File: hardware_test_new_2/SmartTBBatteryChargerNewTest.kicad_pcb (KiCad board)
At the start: 4 copper layers, 100 x 100 mm, 260 parts, among them J10 XT60_MALE, J3 XT60_MALE, J4 XT60_MALE, J5 XT60_MALE, J6 XT60_MALE, J7 Conn_SWD, J8 Conn_01x02, J9 XT60_MALE, Q3 AO3400A, Q4 BSC070N10NS5, Q5 BSC070N10NS5, Q6 BSC070N10NS5, Q7 BSC070N10NS5, Q8 BSC070N10NS5, Q9 BSC070N10NS5, SW1 SW_Push, SW2 SW_Push, SW3 SW_Push, SW4 SW_Push, SW5 SW_Push, SW6 SW_Push, U1 RY8411, U10 INA180A1, U11 INA180A1, U12 FD6288Q, U2 RS3236, U3 RY8411, U4 STM32G474RBTx, U5 INA180A1, U6 FD6288Q, U7 INA180A1, U8 INA180A1, U9 INA180A1

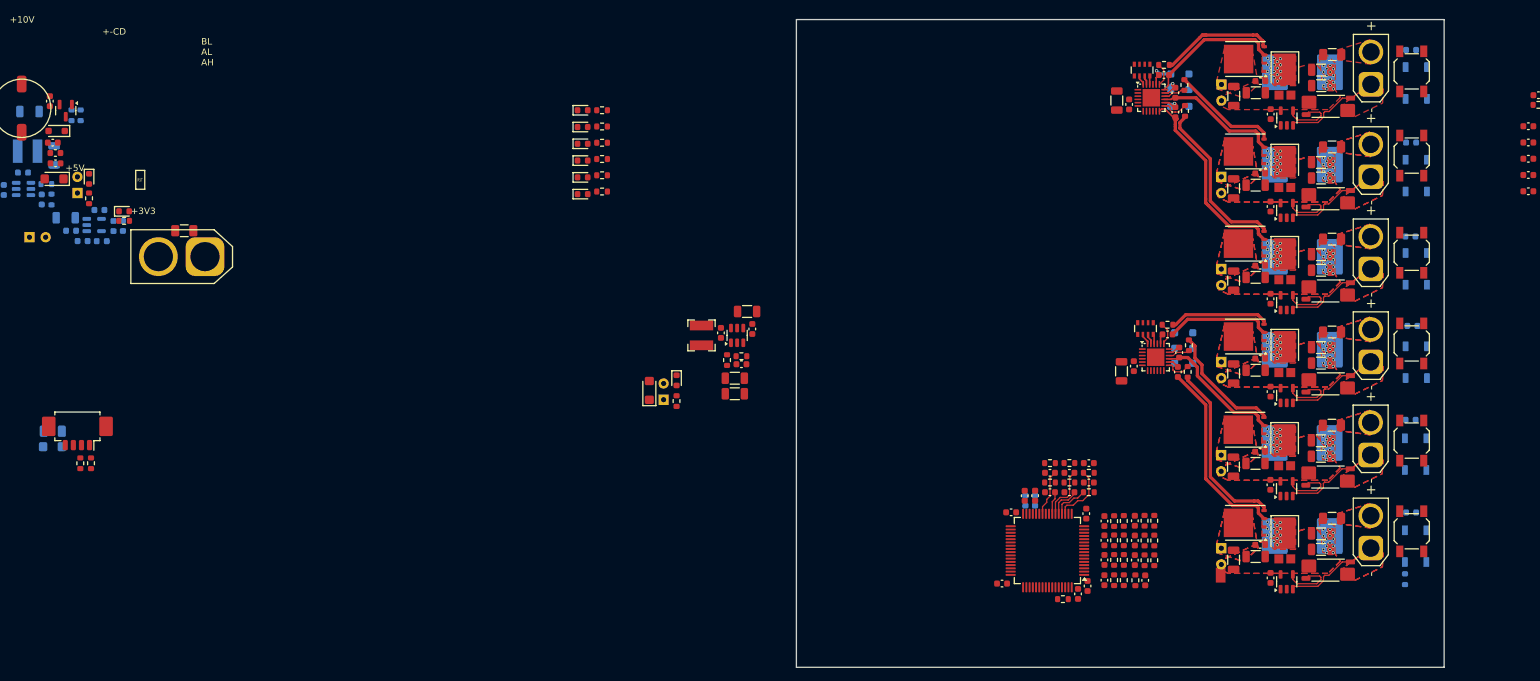
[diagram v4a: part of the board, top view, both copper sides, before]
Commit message: rearrange layout
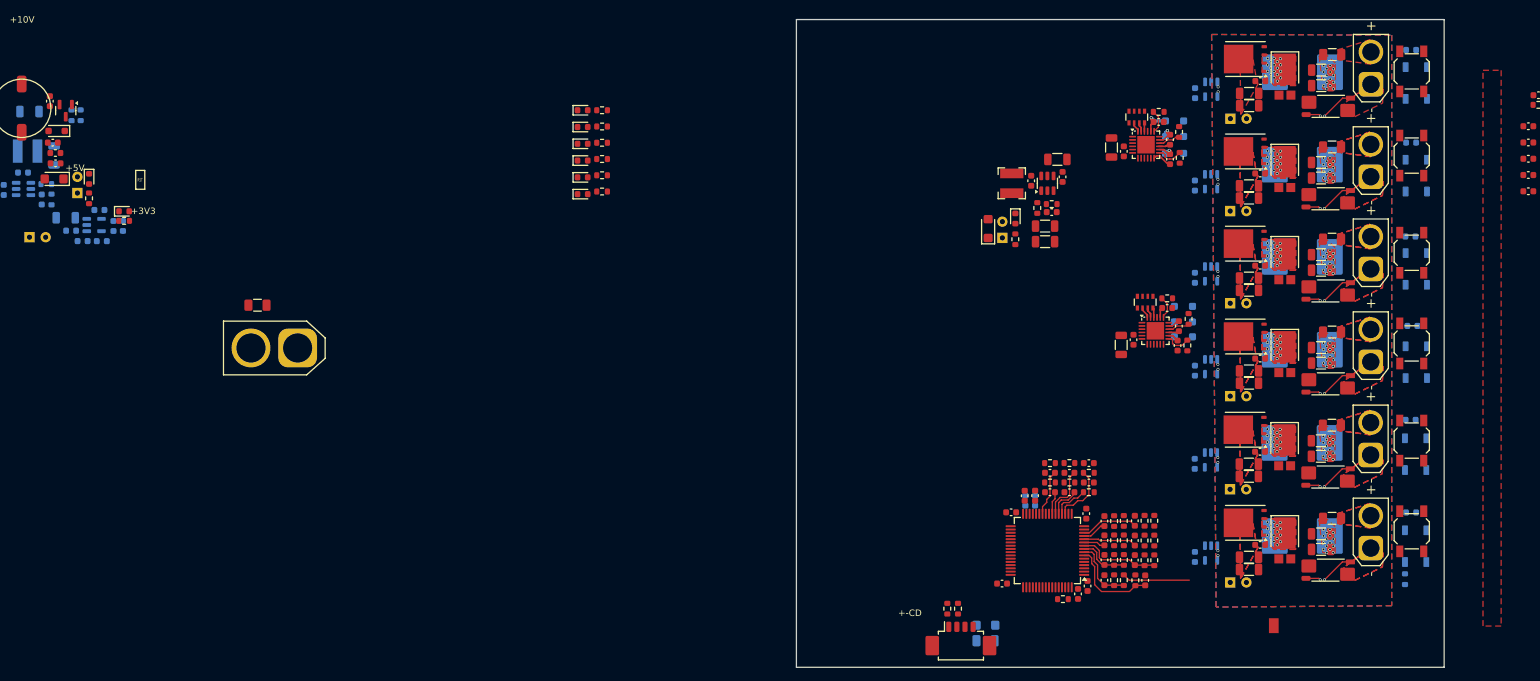
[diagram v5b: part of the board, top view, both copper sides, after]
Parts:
- C44, C51, C67, C84, C85, C86, U10, U11, U5, U7, U8, U9: moved to B.Cu
- moved F7 147.6 mm to (186.2, 147.9), turned to 180 degrees
- moved D15 146.7 mm to (186.2, 145.5), turned to 180 degrees
- moved J7 140.3 mm to (182.4, 148.2), turned to 0 degrees
- moved R36 137.3 mm to (181.9, 142.9), turned to -90 degrees
- moved R37 134.1 mm to (180.3, 142.9), turned to -90 degrees
- moved D17 58.0 mm to (190.8, 82.7)
- moved R19 58.0 mm to (190.8, 85.9)
- moved C20 58.0 mm to (188.8, 85.7)
- moved D1 58.0 mm to (186.6, 84.3)
- moved C1 53.3 mm to (197.3, 73.6)
- moved C14 53.3 mm to (196.4, 81.7)
- moved C16 53.3 mm to (195.4, 86.3)
- moved C6 53.3 mm to (198.1, 76.3)
- moved L1 53.3 mm to (190.2, 77.3)
- moved R1 53.3 mm to (196.4, 80.5)
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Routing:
- net CHC2_SW: track 29.5 -> 0.00 mm
- net Net-(Q9-G): track 27.6 -> 0.00 mm
- net CHB1_SW: track 30.3 -> 3.13 mm
- net Net-(Q6-G): track 25.8 -> 0.00 mm
- net CHA1_SW: track 21.1 -> 0.00 mm
- net Net-(Q8-G): track 18.6 -> 0.00 mm
- net CHC1_SW: track 20.0 -> 1.43 mm
- net Net-(Q4-G): track 17.7 -> 0.00 mm
- net CHA2_SW: track 19.2 -> 1.65 mm
- net Net-(Q5-G): track 16.7 -> 0.00 mm
- net CHB2_SW: track 16.4 -> 0.00 mm
- net Net-(Q7-G): track 15.6 -> 0.00 mm
- net Net-(U4-PG10): track 0.00 -> 14.3 mm
- net CHC1_VS: track 0.00 -> 12.8 mm
- net /ChannelC2/CH_SHUNT+: track 11.2 -> 23.6 mm, vias 0 -> 2
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- added copper zone on B.Cu, net GNDPWR
- added copper zone on In1.Cu, net GNDPWR
- added copper zone on In2.Cu, net GNDPWR
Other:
- board text removed: "BL AL AH"
- board text removed: "V_B"
